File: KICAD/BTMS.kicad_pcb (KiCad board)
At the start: 4 copper layers, 80.1 x 55.8 mm, 151 parts, among them J1 Batt_Ballance, J2 AUX_Charge, J3 Battery_IO, J4 Power_Out, J5 BT_LM62, J6 DSKY, J7 PWR_SW, J8 ICSP, J9 Heater, P1 USB_C_Plug, Q1 SSM3K341R, Q2 DMN65D8L, Q3 SSM3K341R, Q4 FDN340P, Q5 FDN340P, Q6 FDN340P, Q7 DMN65D8L, Q8 DMN65D8L, U1 ACS711xLCTR-25AB, U10 BA033CC0FP-E2, U11 AON7522E, U12 AON7522E, U13 LM62CIM3/NOPB, U14 FAN3100TSX, U15 FAN3100TSX, U16 AON7522E, U17 dsPIC30F3011-PT, U18 FT230XQ, U2 AP33771, U3 IS281-4, U4 Q294700DSGR, U5 SCF4030-12-0X, U6 AONR21321, U7 ACS711xLCTR-25AB, U8 IS281-4, U9 IRS2184

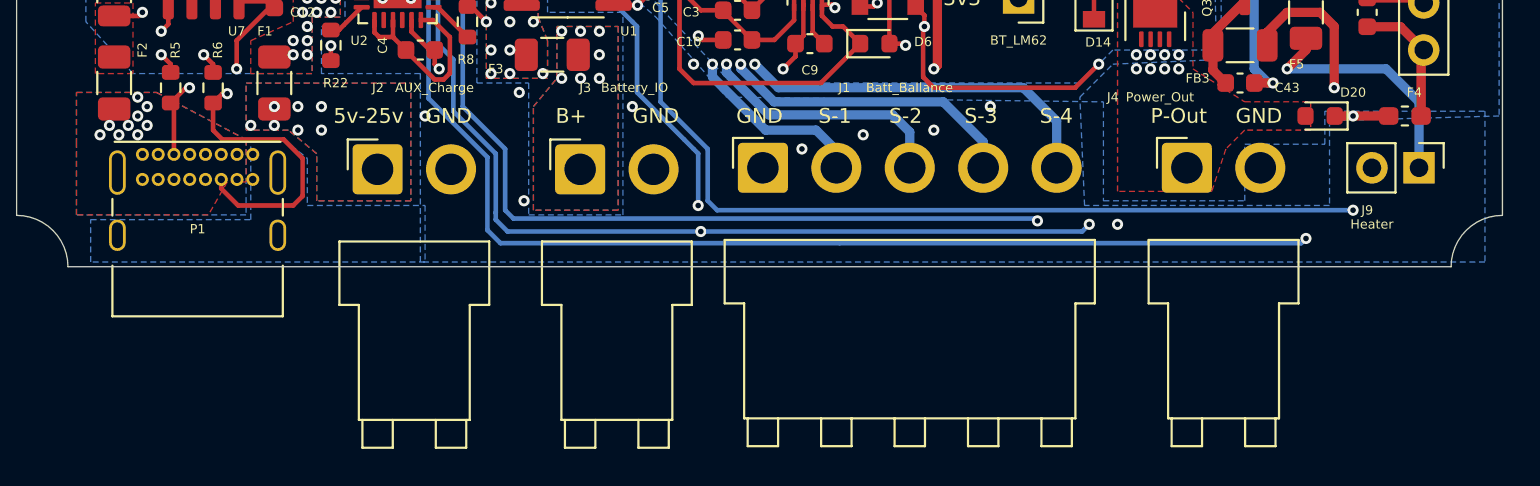
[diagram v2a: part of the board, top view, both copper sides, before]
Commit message: Cleaned up connector silkscreens. No more DRC warnings.
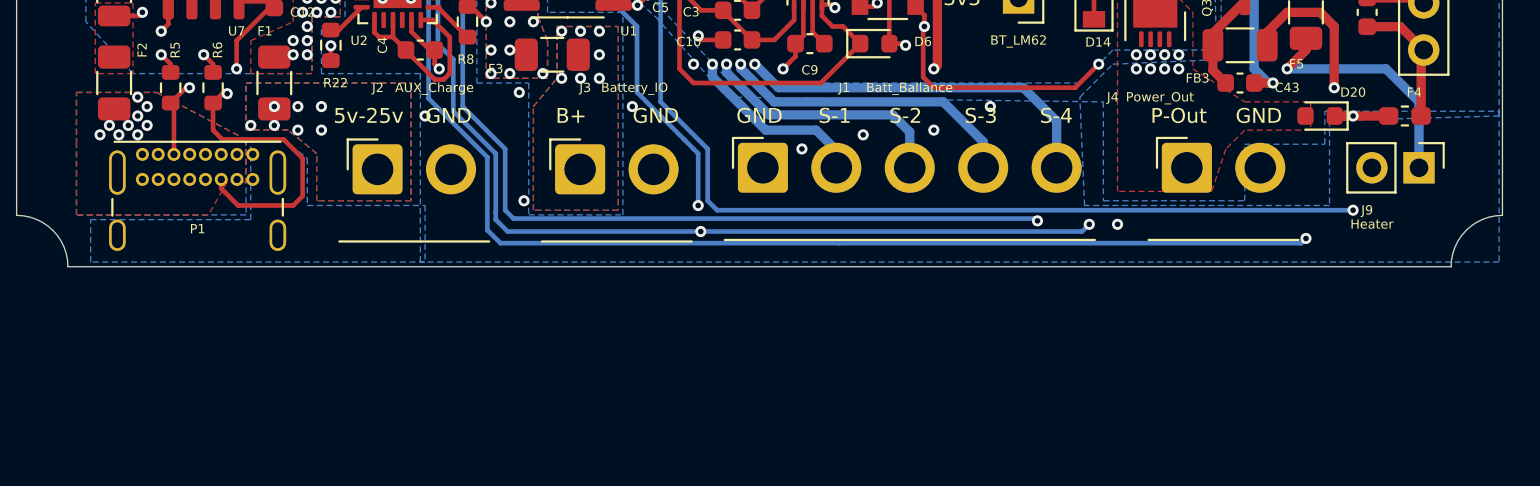
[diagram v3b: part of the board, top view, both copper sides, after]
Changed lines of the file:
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@@
       (effects (font (size 1 1) (thickness 0.15)))
     )
-    (fp_line (start -1.01 13.51) (end -1.01 7.31) (layer "F.SilkS") (width 0.12))
-    (fp_line (start -0.82 13.51) (end -0.82 15.01) (layer "F.SilkS") (width 0.12))
-    (fp_line (start 6.02 3.89) (end 6.02 7.31) (layer "F.SilkS") (width 0.12))
-    (fp_line (start 4.97 7.31) (end 4.97 13.51) (layer "F.SilkS") (width 0.12))
     (fp_line (start -2.06 3.89) (end 6.02 3.89) (layer "F.SilkS") (width 0.12))
-    (fp_line (start 4.78 15.01) (end 4.78 13.51) (layer "F.SilkS") (width 0.12))
-    (fp_line (start -1.01 7.31) (end -2.06 7.31) (layer "F.SilkS") (width 0.12))
-    (fp_line (start -2.06 7.31) (end -2.06 3.89) (layer "F.SilkS") (width 0.12))
-    (fp_line (start 3.14 13.51) (end 3.14 15.01) (layer "F.SilkS") (width 0.12))
-    (fp_line (start 0.82 15.01) (end 0.82 13.51) (layer "F.SilkS") (width 0.12))
-    (fp_line (start -0.82 15.01) (end 0.82 15.01) (layer "F.SilkS") (width 0.12))
-    (fp_line (start 6.02 7.31) (end 4.97 7.31) (layer "F.SilkS") (width 0.12))
     (fp_line (start -1.61 -1.61) (end -1.61 0) (layer "F.SilkS") (width 0.12))
-    (fp_line (start 3.14 15.01) (end 4.78 15.01) (layer "F.SilkS") (width 0.12))
-    (fp_line (start 4.97 13.51) (end -1.01 13.51) (layer "F.SilkS") (width 0.12))
     (fp_line (start 0 -1.61) (end -1.61 -1.61) (layer "F.SilkS") (width 0.12))
     (fp_line (start 6.41 -1.85) (end -2.45 -1.85) (layer "F.CrtYd") (width 0.05))
@@
       (effects (font (size 1 1) (thickness 0.15)))
     )
-    (fp_line (start -1.62 8.73) (end 7.57 8.73) (layer "F.SilkS") (width 0.12))
     (fp_line (start -1.62 2.4) (end -1.62 3.3) (layer "F.SilkS") (width 0.12))
-    (fp_line (start 7.57 6) (end 7.57 8.73) (layer "F.SilkS") (width 0.12))
     (fp_line (start 7.57 2.4) (end 7.57 3.3) (layer "F.SilkS") (width 0.12))
     (fp_line (start -1.5 -0.68) (end 7.45 -0.68) (layer "F.SilkS") (width 0.12))
-    (fp_line (start -1.62 6) (end -1.62 8.73) (layer "F.SilkS") (width 0.12))
     (fp_line (start -2.3 -1.06) (end -2.3 9.11) (layer "F.CrtYd") (width 0.05))
     (fp_line (start -2.3 9.11) (end 8.25 9.11) (layer "F.CrtYd") (width 0.05))
@@
       (effects (font (size 0.5 0.5) (thickness 0.15)))
     )
-    (fp_text user "${REFERENCE}" (at 1.98 9.45) (layer "F.Fab")
-      (effects (font (size 1 1) (thickness 0.15)))
-    )
-    (fp_line (start -1.01 7.31) (end -2.06 7.31) (layer "F.SilkS") (width 0.12))
-    (fp_line (start 6.02 3.89) (end 6.02 7.31) (layer "F.SilkS") (width 0.12))
-    (fp_line (start -0.82 13.51) (end -0.82 15.01) (layer "F.SilkS") (width 0.12))
     (fp_line (start -2.06 3.89) (end 6.02 3.89) (layer "F.SilkS") (width 0.12))
     (fp_line (start -1.61 -1.61) (end -1.61 0) (layer "F.SilkS") (width 0.12))
-    (fp_line (start 3.14 13.51) (end 3.14 15.01) (layer "F.SilkS") (width 0.12))
-    (fp_line (start 4.97 13.51) (end -1.01 13.51) (layer "F.SilkS") (width 0.12))
-    (fp_line (start 6.02 7.31) (end 4.97 7.31) (layer "F.SilkS") (width 0.12))
-    (fp_line (start -2.06 7.31) (end -2.06 3.89) (layer "F.SilkS") (width 0.12))
-    (fp_line (start -0.82 15.01) (end 0.82 15.01) (layer "F.SilkS") (width 0.12))
-    (fp_line (start 0.82 15.01) (end 0.82 13.51) (layer "F.SilkS") (width 0.12))
     (fp_line (start 0 -1.61) (end -1.61 -1.61) (layer "F.SilkS") (width 0.12))
-    (fp_line (start 4.97 7.31) (end 4.97 13.51) (layer "F.SilkS") (width 0.12))
-    (fp_line (start 4.78 15.01) (end 4.78 13.51) (layer "F.SilkS") (width 0.12))
-    (fp_line (start 3.14 15.01) (end 4.78 15.01) (layer "F.SilkS") (width 0.12))
-    (fp_line (start -1.01 13.51) (end -1.01 7.31) (layer "F.SilkS") (width 0.12))
     (fp_line (start -2.45 -1.85) (end -2.45 15.4) (layer "F.CrtYd") (width 0.05))
     (fp_line (start 6.41 15.4) (end 6.41 -1.85) (layer "F.CrtYd") (width 0.05))
@@
       (effects (font (size 1 1) (thickness 0.15)))
     )
-    (fp_line (start 6.02 3.89) (end 6.02 7.31) (layer "F.SilkS") (width 0.12))
-    (fp_line (start 0.82 15.01) (end 0.82 13.51) (layer "F.SilkS") (width 0.12))
-    (fp_line (start -0.82 13.51) (end -0.82 15.01) (layer "F.SilkS") (width 0.12))
-    (fp_line (start 4.97 13.51) (end -1.01 13.51) (layer "F.SilkS") (width 0.12))
-    (fp_line (start -1.01 13.51) (end -1.01 7.31) (layer "F.SilkS") (width 0.12))
-    (fp_line (start -2.06 7.31) (end -2.06 3.89) (layer "F.SilkS") (width 0.12))
     (fp_line (start 0 -1.61) (end -1.61 -1.61) (layer "F.SilkS") (width 0.12))
-    (fp_line (start 4.97 7.31) (end 4.97 13.51) (layer "F.SilkS") (width 0.12))
-    (fp_line (start -1.01 7.31) (end -2.06 7.31) (layer "F.SilkS") (width 0.12))
-    (fp_line (start 3.14 15.01) (end 4.78 15.01) (layer "F.SilkS") (width 0.12))
-    (fp_line (start 4.78 15.01) (end 4.78 13.51) (layer "F.SilkS") (width 0.12))
-    (fp_line (start -0.82 15.01) (end 0.82 15.01) (layer "F.SilkS") (width 0.12))
-    (fp_line (start 3.14 13.51) (end 3.14 15.01) (layer "F.SilkS") (width 0.12))
-    (fp_line (start 6.02 7.31) (end 4.97 7.31) (layer "F.SilkS") (width 0.12))
     (fp_line (start -1.61 -1.61) (end -1.61 0) (layer "F.SilkS") (width 0.12))
     (fp_line (start -2.06 3.89) (end 6.02 3.89) (layer "F.SilkS") (width 0.12))
@@
       (effects (font (size 1 1) (thickness 0.15)))
     )
-    (fp_line (start 15.02 13.51) (end 15.02 15.01) (layer "F.SilkS") (width 0.12))
-    (fp_line (start 8.74 15.01) (end 8.74 13.51) (layer "F.SilkS") (width 0.12))
-    (fp_line (start -0.82 15.01) (end 0.82 15.01) (layer "F.SilkS") (width 0.12))
-    (fp_line (start 16.85 7.31) (end 16.85 13.51) (layer "F.SilkS") (width 0.12))
-    (fp_line (start 11.06 15.01) (end 12.7 15.01) (layer "F.SilkS") (width 0.12))
-    (fp_line (start 4.78 15.01) (end 4.78 13.51) (layer "F.SilkS") (width 0.12))
-    (fp_line (start -2.06 7.31) (end -2.06 3.89) (layer "F.SilkS") (width 0.12))
-    (fp_line (start 3.14 13.51) (end 3.14 15.01) (layer "F.SilkS") (width 0.12))
-    (fp_line (start 16.85 13.51) (end -1.01 13.51) (layer "F.SilkS") (width 0.12))
-    (fp_line (start 16.66 15.01) (end 16.66 13.51) (layer "F.SilkS") (width 0.12))
-    (fp_line (start 7.1 13.51) (end 7.1 15.01) (layer "F.SilkS") (width 0.12))
-    (fp_line (start 17.9 7.31) (end 16.85 7.31) (layer "F.SilkS") (width 0.12))
-    (fp_line (start 7.1 15.01) (end 8.74 15.01) (layer "F.SilkS") (width 0.12))
-    (fp_line (start 3.14 15.01) (end 4.78 15.01) (layer "F.SilkS") (width 0.12))
     (fp_line (start -1.61 -1.61) (end -1.61 0) (layer "F.SilkS") (width 0.12))
-    (fp_line (start 12.7 15.01) (end 12.7 13.51) (layer "F.SilkS") (width 0.12))
-    (fp_line (start -0.82 13.51) (end -0.82 15.01) (layer "F.SilkS") (width 0.12))
-    (fp_line (start 17.9 3.89) (end 17.9 7.31) (layer "F.SilkS") (width 0.12))
     (fp_line (start 0 -1.61) (end -1.61 -1.61) (layer "F.SilkS") (width 0.12))
-    (fp_line (start -1.01 7.31) (end -2.06 7.31) (layer "F.SilkS") (width 0.12))
-    (fp_line (start 11.06 13.51) (end 11.06 15.01) (layer "F.SilkS") (width 0.12))
-    (fp_line (start 15.02 15.01) (end 16.66 15.01) (layer "F.SilkS") (width 0.12))
-    (fp_line (start 0.82 15.01) (end 0.82 13.51) (layer "F.SilkS") (width 0.12))
     (fp_line (start -2.06 3.89) (end 17.9 3.89) (layer "F.SilkS") (width 0.12))
-    (fp_line (start -1.01 13.51) (end -1.01 7.31) (layer "F.SilkS") (width 0.12))
     (fp_line (start -2.45 15.4) (end 18.29 15.4) (layer "F.CrtYd") (width 0.05))
     (fp_line (start 18.29 15.4) (end 18.29 -1.85) (layer "F.CrtYd") (width 0.05))
@@
         (xy 179.07 144.272)
         (xy 179.07 142.494)
-        (xy 187.706 142.494)
-        (xy 187.706 150.622)
+        (xy 188.468 142.494)
+        (xy 188.468 150.622)
         (xy 130.302 150.622)
         (xy 130.302 140.462)

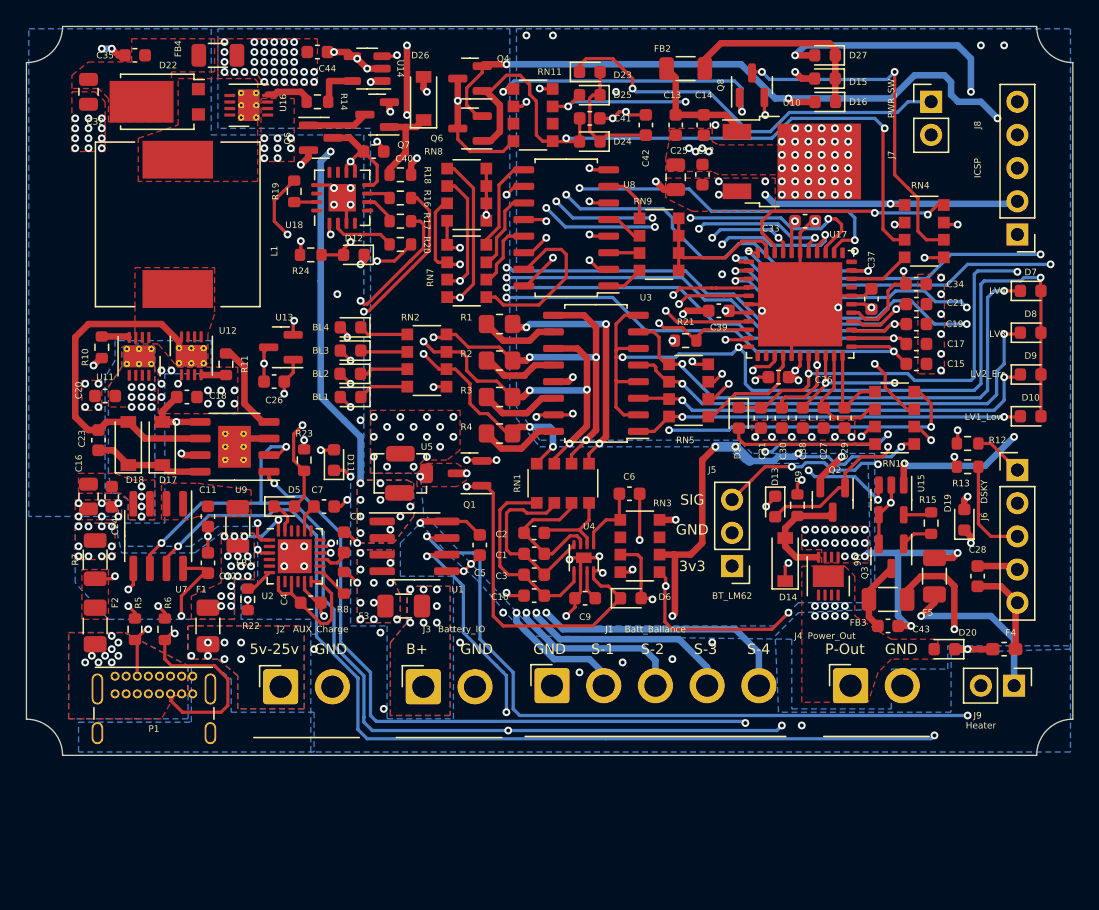
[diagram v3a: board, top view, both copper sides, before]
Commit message: Added groundplanes to front and middle layer. Cleaned up islands and tails.
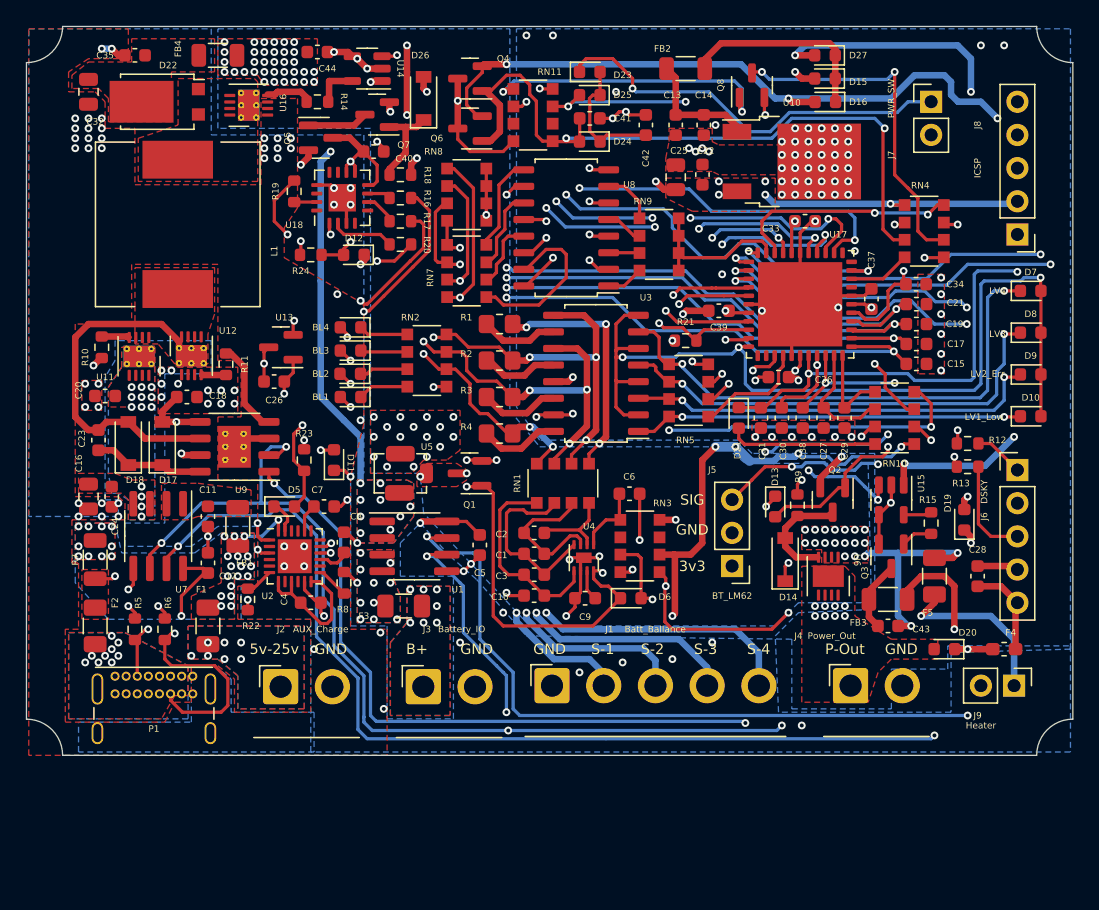
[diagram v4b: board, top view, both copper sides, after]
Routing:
- net /LBatt_Cell_1: track 69.5 -> 68.7 mm
- added copper zone on In2.Cu, net GND

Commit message: Added solder mask and solder paste lines for high-current traces.
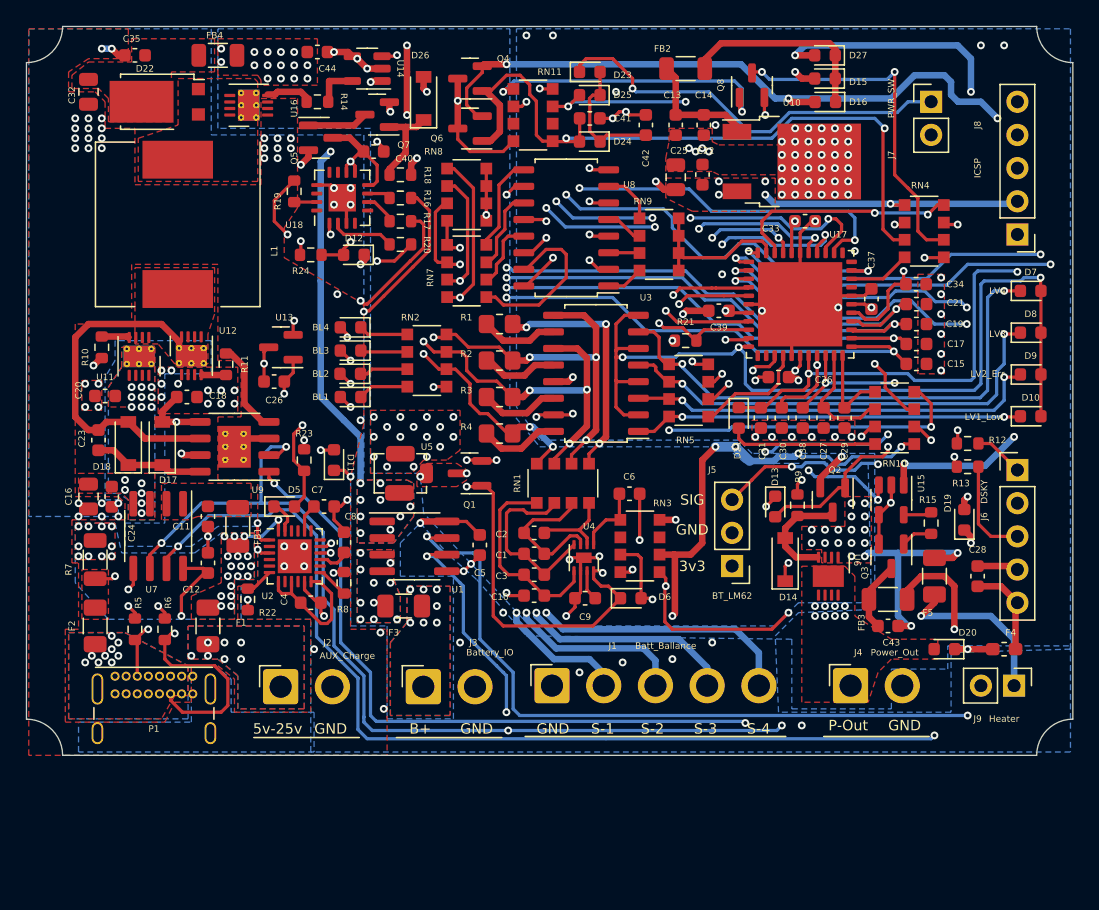
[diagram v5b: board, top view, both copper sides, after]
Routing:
- net GND: track 109.2 -> 109.4 mm, vias 169 -> 168
- net Net-(C16-Pad1): vias 13 -> 15
- net /ExtBus: vias 71 -> 51

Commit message: Cleaned up some things.
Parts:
- moved C33 0.76 mm to (168.9, 110.0)
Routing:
- net +5C: track 213.2 -> 215.3 mm, vias 23 -> 22
- net GND: track 109.4 -> 110.9 mm
